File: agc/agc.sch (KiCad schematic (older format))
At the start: 114 parts, among them J1 SMA_DAC, J2 SMA_LPTR, J3 SMA_DRIVER, J4 SMA_RX, K1 TR, K2 CONN_3, K3 VIN, K4 CONN_3, K5 TR, K6 TR, K7 HVMON, P1 COUPLED_TEST, P2 FWD_FAULT, P3 REF_FAULT, P4 REF_FAULT, U1 BA08CC0WFP, U10 74AHC1G04, U11 75182, U12 78SRH-5/2-C, U2 HMC475, U3 HMC595, U4 HMC595, U5 HMC595, U8 MGA-61563, U9 LTC2914-2

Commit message: updated component values for driver, agc, and tr switch
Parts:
- C2: value CAPAPOL -> 47uF
- L1: value 22uH -> 10uH
- L5: value INDUCTOR_SMALL -> 270nH
- R33: value 44k2 -> 68.1k
- R34, R37: value 1k -> 6.34k
- R35, R38, R44: value 4k53 -> 5.1k
- R36: value 300 -> 68.1k
- R42: value 44k2 -> 1.91M
- R43: value 1k -> 3.3k
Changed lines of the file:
@@
 P 11700 1950
 F 0 "L5" H 11700 2050 50  0000 C CNN
-F 1 "INDUCTOR_SMALL" H 11700 1900 50  0000 C CNN
+F 1 "270nH" H 11700 1900 50  0000 C CNN
 F 2 "SMD_Packages:SM0805" H 11700 1950 60  0001 C CNN
 F 3 "" H 11700 1950 60  0000 C CNN
@@
 P 2350 11450
 F 0 "L1" H 2350 11550 50  0000 C CNN
-F 1 "22uH" H 2350 11400 50  0000 C CNN
+F 1 "10uH" H 2350 11400 50  0000 C CNN
 F 2 "Inductors:SELF-WE-TPC_M" H 2350 11450 60  0001 C CNN
 F 3 "" H 2350 11450 60  0000 C CNN
@@
 P 2800 11900
 F 0 "C2" H 2850 12000 40  0000 L CNN
-F 1 "CAPAPOL" H 2850 11800 40  0000 L CNN
+F 1 "47uF" H 2850 11800 40  0000 L CNN
 F 2 "SMD_Packages:SM1206POL" H 2900 11750 30  0001 C CNN
 F 3 "" H 2800 11900 300 0000 C CNN
@@
 P 16850 9000
 F 0 "R33" V 16930 9000 40  0000 C CNN
-F 1 "44k2" V 16857 9001 40  0000 C CNN
+F 1 "68.1k" V 16857 9001 40  0000 C CNN
 F 2 "SMD_Packages:SM0805" V 16780 9000 30  0001 C CNN
 F 3 "" H 16850 9000 30  0000 C CNN
@@
 P 16850 11500
 F 0 "R35" V 16930 11500 40  0000 C CNN
-F 1 "4k53" V 16857 11501 40  0000 C CNN
+F 1 "5.1k" V 16857 11501 40  0000 C CNN
 F 2 "SMD_Packages:SM0805" V 16780 11500 30  0001 C CNN
 F 3 "" H 16850 11500 30  0000 C CNN
@@
 P 16850 9850
 F 0 "R34" V 16930 9850 40  0000 C CNN
-F 1 "1k" V 16857 9851 40  0000 C CNN
+F 1 "6.34k" V 16857 9851 40  0000 C CNN
 F 2 "SMD_Packages:SM0805" V 16780 9850 30  0001 C CNN
 F 3 "" H 16850 9850 30  0000 C CNN
@@
 P 17100 9000
 F 0 "R36" V 17180 9000 40  0000 C CNN
-F 1 "300" V 17107 9001 40  0000 C CNN
+F 1 "68.1k" V 17107 9001 40  0000 C CNN
 F 2 "SMD_Packages:SM0805" V 17030 9000 30  0001 C CNN
 F 3 "" H 17100 9000 30  0000 C CNN
@@
 P 17100 11500
 F 0 "R38" V 17180 11500 40  0000 C CNN
-F 1 "4k53" V 17107 11501 40  0000 C CNN
+F 1 "5.1k" V 17107 11501 40  0000 C CNN
 F 2 "SMD_Packages:SM0805" V 17030 11500 30  0001 C CNN
 F 3 "" H 17100 11500 30  0000 C CNN
@@
 P 17100 9850
 F 0 "R37" V 17180 9850 40  0000 C CNN
-F 1 "1k" V 17107 9851 40  0000 C CNN
+F 1 "6.34k" V 17107 9851 40  0000 C CNN
 F 2 "SMD_Packages:SM0805" V 17030 9850 30  0001 C CNN
 F 3 "" H 17100 9850 30  0000 C CNN
@@
 P 17600 9850
 F 0 "R43" V 17680 9850 40  0000 C CNN
-F 1 "1k" V 17607 9851 40  0000 C CNN
+F 1 "3.3k" V 17607 9851 40  0000 C CNN
 F 2 "SMD_Packages:SM0805" V 17530 9850 30  0001 C CNN
 F 3 "" H 17600 9850 30  0000 C CNN
@@
 P 17600 11500
 F 0 "R44" V 17680 11500 40  0000 C CNN
-F 1 "4k53" V 17607 11501 40  0000 C CNN
+F 1 "5.1k" V 17607 11501 40  0000 C CNN
 F 2 "SMD_Packages:SM0805" V 17530 11500 30  0001 C CNN
 F 3 "" H 17600 11500 30  0000 C CNN
@@
 P 17600 9000
 F 0 "R42" V 17680 9000 40  0000 C CNN
-F 1 "44k2" V 17607 9001 40  0000 C CNN
+F 1 "1.91M" V 17607 9001 40  0000 C CNN
 F 2 "SMD_Packages:SM0805" V 17530 9000 30  0001 C CNN
 F 3 "" H 17600 9000 30  0000 C CNN

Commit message: fixed layout bugs in r1 (agc r2 incomplete)
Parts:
- removed R51: 0, SMD_Packages:SM0805, symbol R
- added C16, C18, C21: 10nF, SMD_Packages:SM0805, symbol C
- added JP1: JUMPER3, Connect:bornier3, symbol JUMPER3
- added JP2: JUMPER, Connect:bornier2, symbol JUMPER
- added P5, P6, P7, P8, P9: COUPLED_TEST, Connect:PINTST, symbol CONN_1
- added R18: 10k, SMD_Packages:SM0805, symbol R
- added U6: 74AHC1G04, SMD_Packages:SOT23-5, symbol 74AHC1G04
- D1, D2: footprint LEDs:LED-0805 -> Diodes_SMD:Diode-SMB_Handsoldering
- K1, K2, K3, K4, K5, K6, K7: footprint Connect:SIL-3 -> Connect:PINHEAD1-3
- L3, L5: value 270nH -> 10uH; footprint SMD_Packages:SM0805 -> SMD_Packages:SM1210
- P2, P3, P4: footprint Connect:SIL-4 -> Connect:bornier4
- R45: value 300 -> 10k
- R46, R47: value 300 -> 1k
- U1: footprint SMD_Packages:DPAK5 -> to252_5:TO252-5
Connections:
- net +5V: now also D4.1 (A), C21.2, JP2.1, P5.1, R18.1, U6.5 (VCC)
- net FAULT: now also P9.1, R18.2; no longer D4.2 (K)
- net GND: now also U3.2 (GND), C16.2, C18.2, C21.1, JP1.1, P7.1, U6.3 (GND); no longer R15.1, R16.1
- net TX: now also U6.4
- net VCC: now also P6.1
- net at C13.1, C9.1, R12.1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: now also D3.1 (A)
- net at R47.2: now also D4.2 (K); no longer D4.1 (A)
- net at R46.2: now also D3.2 (K); no longer D3.1 (A)
- net at U9.11 (~OV): now also P8.1; no longer D3.2 (K)
- net at R45.1, U9.13 (DIS): now also JP2.2
- net at R54.2, U11.6 (1OUT): now also JP1.3; no longer U10.2
- net at R50.1, U10.4: now also U6.2
- new net: C18.1, R16.1
- new net: C16.1, R15.1
- new net: JP1.2, U10.2
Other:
- note added: "buffer 75182, only 3.5V output.."
- moved on the sheet: C28, D3, D4, R45, R46, R47

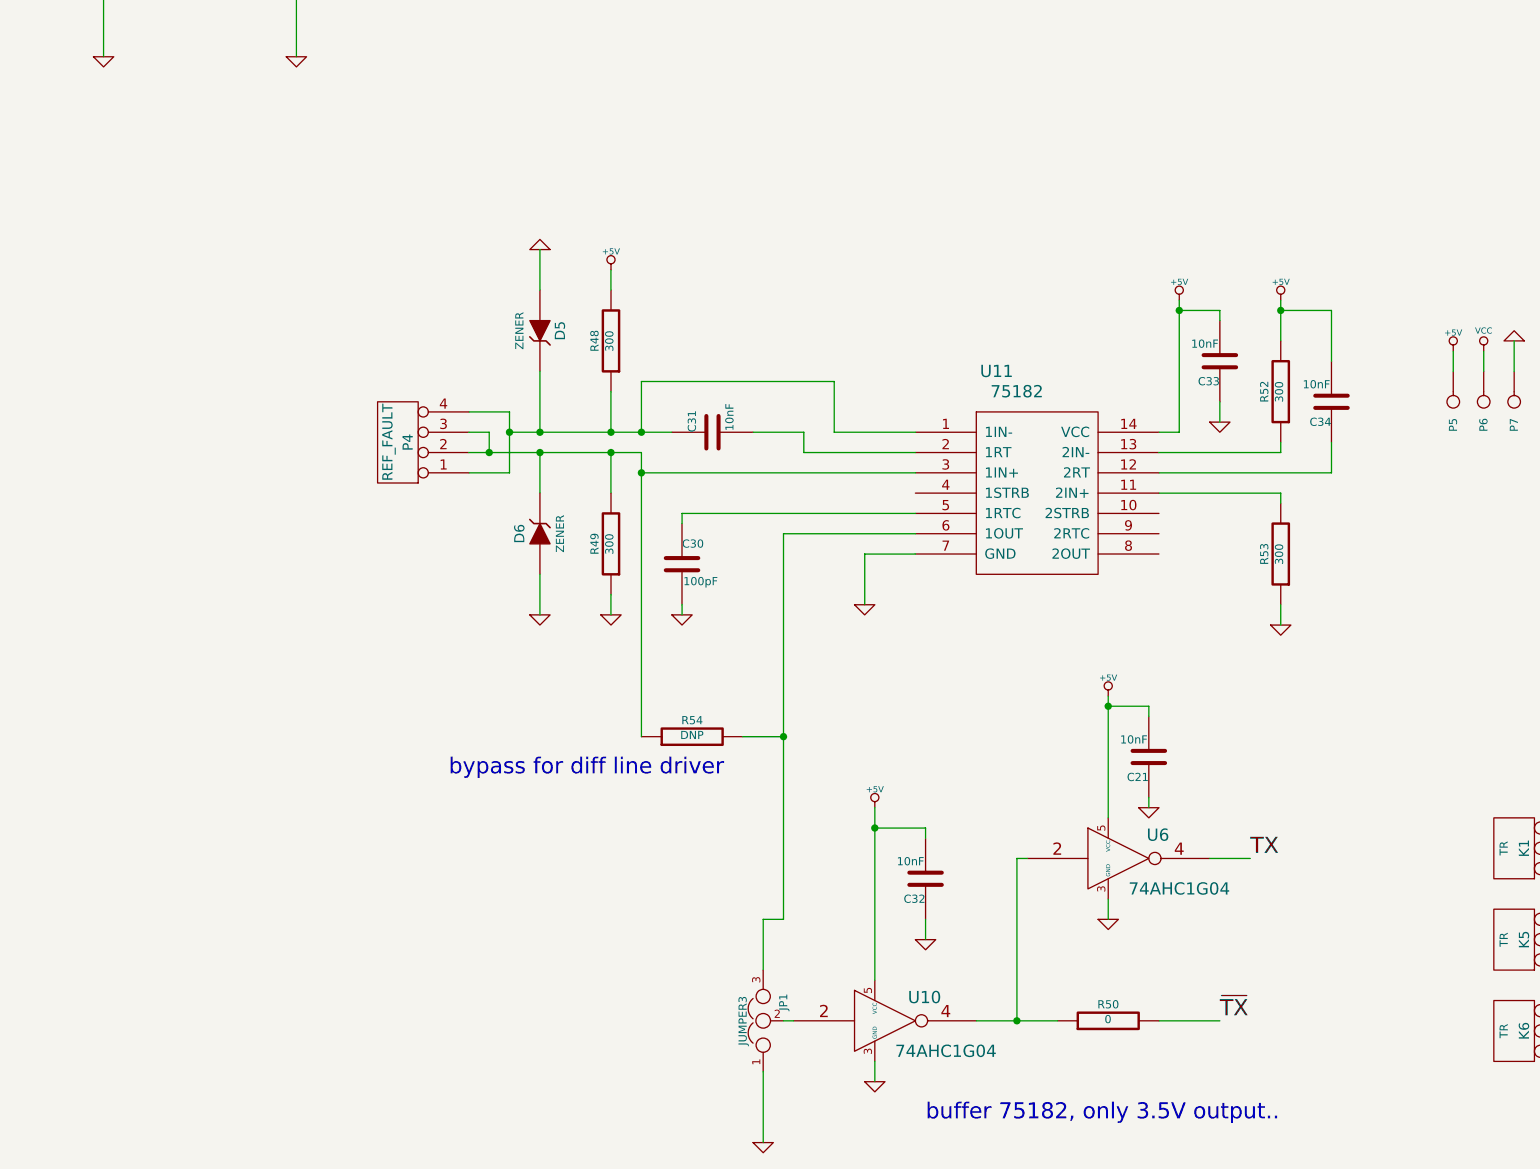
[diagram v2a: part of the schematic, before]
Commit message: added antenna polarization selecter board
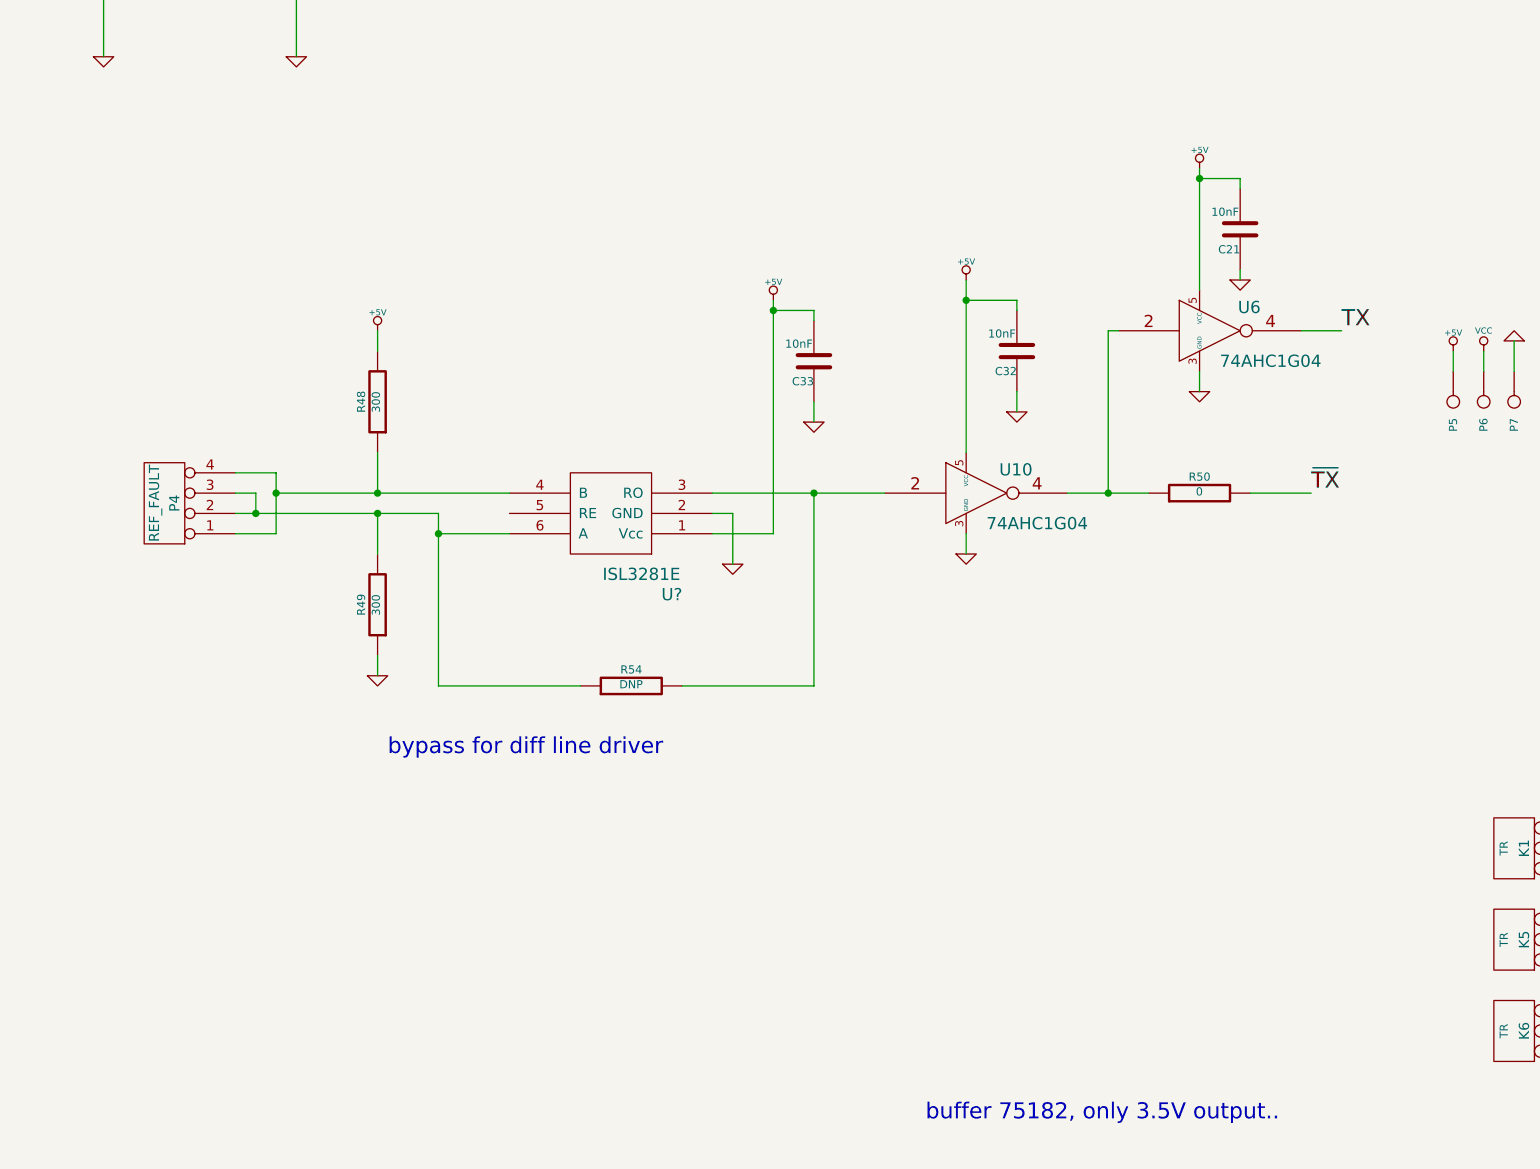
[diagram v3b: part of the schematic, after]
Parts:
- removed C30: 100pF, SMD_Packages:SM0805, symbol C
- removed C31, C34: 10nF, SMD_Packages:SM0805, symbol C
- removed D5, D6: ZENER, Diodes_SMD:Diode-SMB_Handsoldering, symbol ZENER
- removed JP1: JUMPER3, Connect:bornier3, symbol JUMPER3
- removed R52, R53: 300, SMD_Packages:SM0805, symbol R
- removed U11: 75182, SOIC_Packages:SOIC-14_Narrow, symbol 75182
- added U?: ISL3281E, symbol ISL3281E
- P6: value COUPLED_TEST -> TP_VCC
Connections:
- net +5V: now also U?.1 (Vcc)
- net GND: now also U?.2 (GND)
- net at P4.1 (P1), P4.4 (P4), R48.1: now also U?.4 (B)
- net at P4.2 (P2), P4.3 (P3), R49.2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: now also U?.6 (A)
- net at R54.2: now also U10.2, U?.3 (RO)
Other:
- moved on the sheet: C21, C32, C33, P4, R48, R49, R50, R54, U10, U6

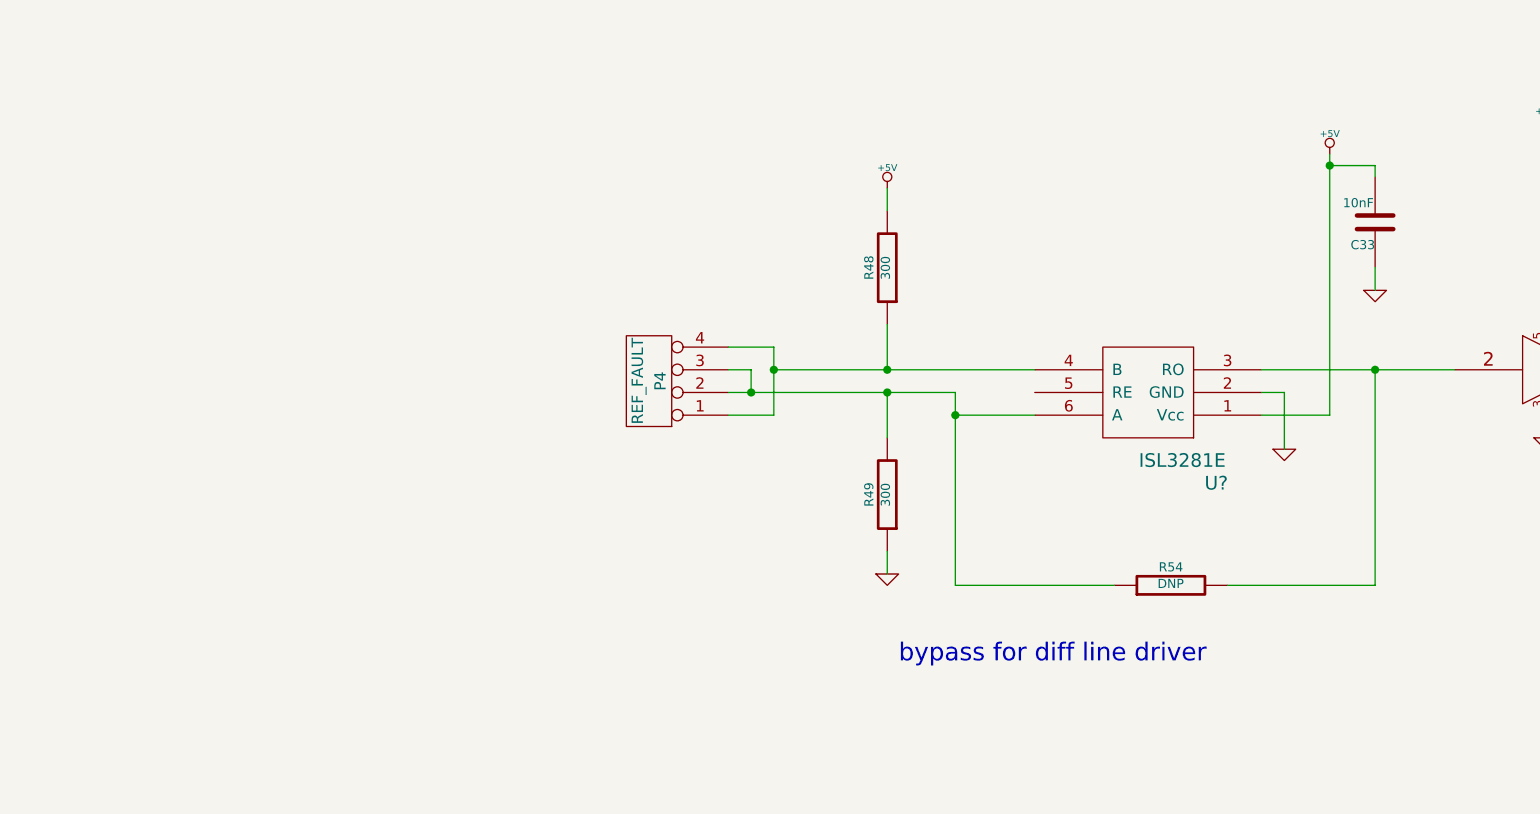
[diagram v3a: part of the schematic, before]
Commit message: updated agc board with lower noise diff receiver
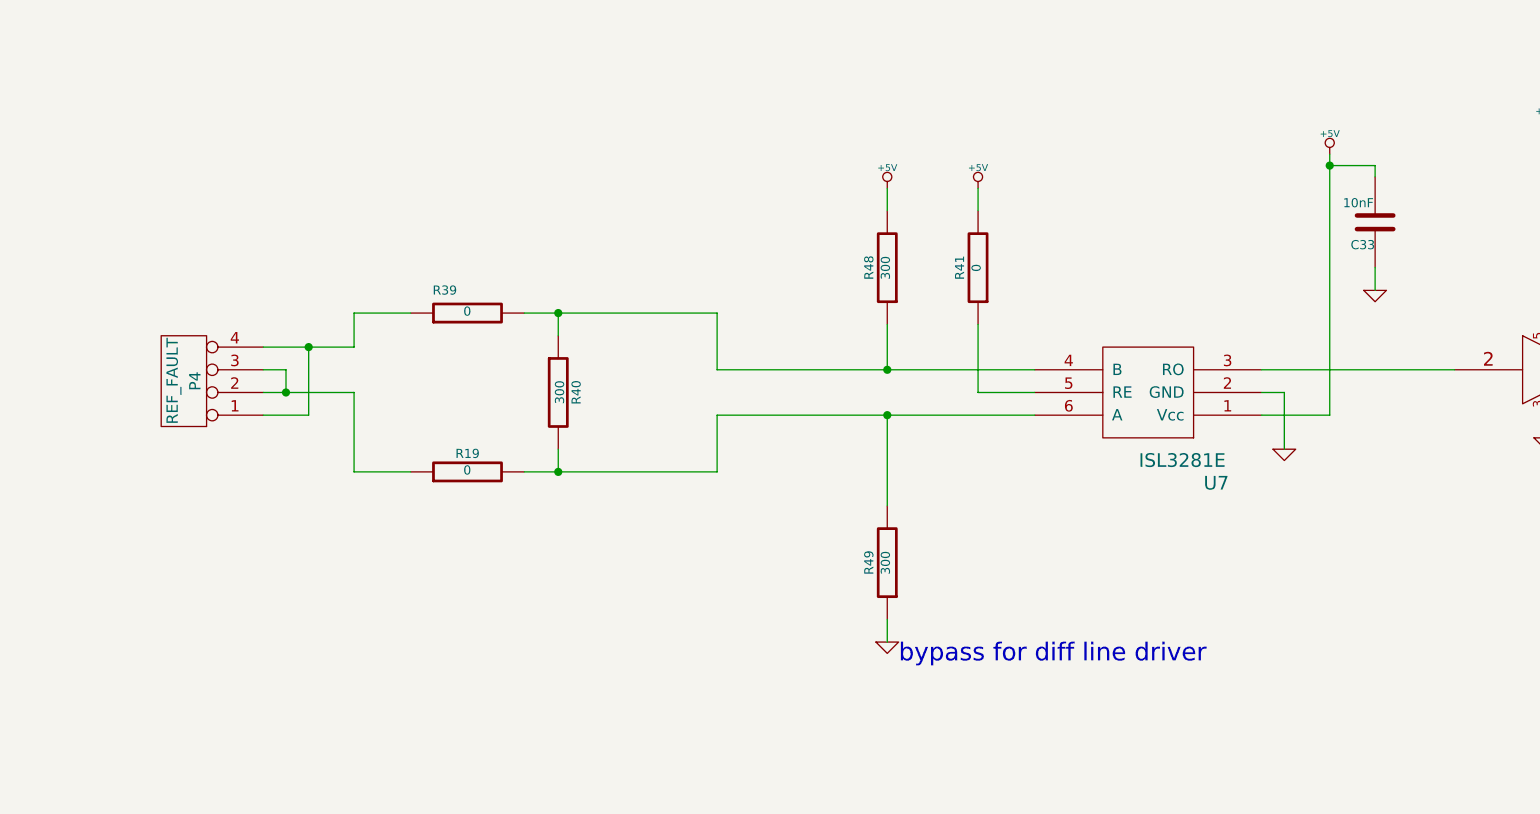
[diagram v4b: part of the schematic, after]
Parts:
- removed R54: DNP, SMD_Packages:SM0805, symbol R
- added R19, R39, R41: 0, SMD_Packages:SM0805, symbol R
- added R40: 300, SMD_Packages:SM0805, symbol R
- JP2: footprint Connect:bornier2 -> Connect:PINHEAD1-2
- P2, P3, P4: footprint Connect:bornier4 -> localconn:conn4
- U7: renamed from U?; footprint (none) -> SMD_Packages:SOT23_6
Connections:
- net +5V: now also R41.2
- net at R49.2, U7.6 (A): now also R19.2, R40.2; no longer P4.2 (P2), P4.3 (P3)
- net at R48.1, U7.4 (B): now also R39.2, R40.1; no longer P4.1 (P1), P4.4 (P4)
- net at U7.5 (RE): now also R41.1
- new net: P4.1 (P1), P4.4 (P4), R39.1
- new net: P4.2 (P2), P4.3 (P3), R19.1
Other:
- moved on the sheet: P4, R49

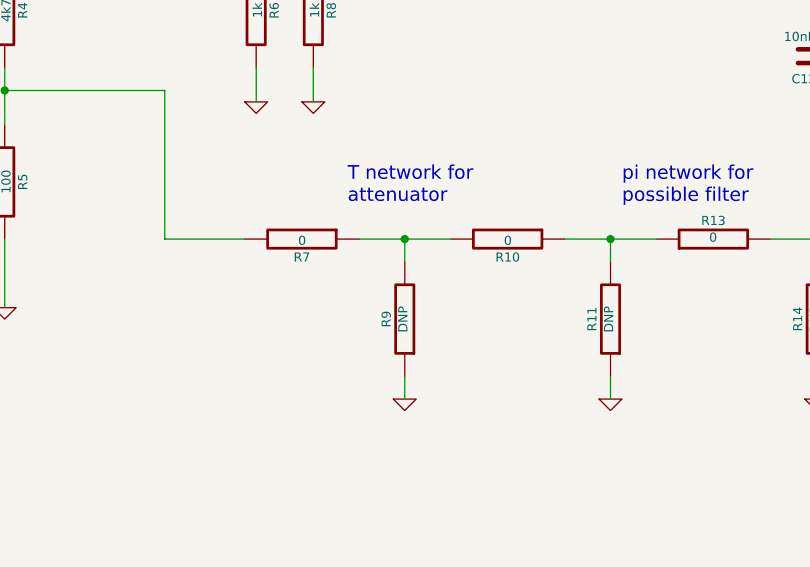
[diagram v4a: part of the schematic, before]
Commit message: added drawing of proposed kodiak transmitter layout
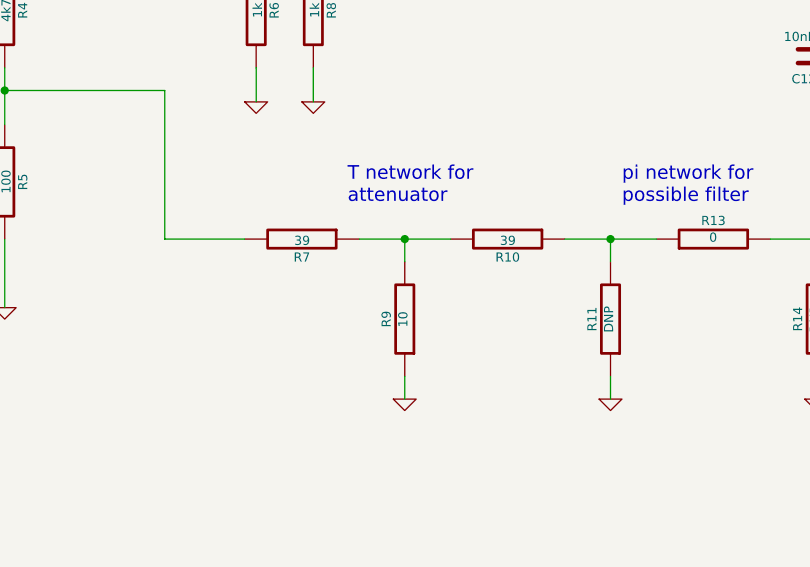
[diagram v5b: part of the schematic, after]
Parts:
- R10, R7: value 0 -> 39
- R9: value DNP -> 10
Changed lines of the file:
@@
 P 4500 4100
 F 0 "R7" V 4580 4100 40  0000 C CNN
-F 1 "0" V 4507 4101 40  0000 C CNN
+F 1 "39" V 4507 4101 40  0000 C CNN
 F 2 "SMD_Packages:SM1206" V 4430 4100 30  0001 C CNN
 F 3 "" H 4500 4100 30  0000 C CNN
@@
 P 4950 4450
 F 0 "R9" V 5030 4450 40  0000 C CNN
-F 1 "DNP" V 4957 4451 40  0000 C CNN
+F 1 "10" V 4957 4451 40  0000 C CNN
 F 2 "SMD_Packages:SM1206" V 4880 4450 30  0001 C CNN
 F 3 "" H 4950 4450 30  0000 C CNN
@@
 P 5400 4100
 F 0 "R10" V 5480 4100 40  0000 C CNN
-F 1 "0" V 5407 4101 40  0000 C CNN
+F 1 "39" V 5407 4101 40  0000 C CNN
 F 2 "SMD_Packages:SM1206" V 5330 4100 30  0001 C CNN
 F 3 "" H 5400 4100 30  0000 C CNN
